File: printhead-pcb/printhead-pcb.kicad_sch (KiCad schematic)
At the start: 22 parts, among them Q1 2N3819, Q2 BSS138, Q3 2N3819, Q4 BSS138, U1 NE555D, U2 NE555D

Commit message: power fans, sensors
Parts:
- removed C1, C4, C6: 100n, Capacitor_SMD:C_0603_1608Metric, symbol Device:C
- removed C2, C5: 700p, Capacitor_SMD:C_0603_1608Metric, symbol Device:C
- removed C3: 2.2u, Capacitor_SMD:C_1210_3225Metric, symbol Device:C
- removed D1, D2, D3, D4: 1N4148W, Diode_SMD:D_SOD-123, symbol Diode:1N4148W
- removed Q1, Q3: 2N3819, Package_DIP:DIP-8_W7.62mm_SMDSocket_SmallPads, symbol Transistor_FET:2N3819
- removed Q2, Q4: BSS138, Package_TO_SOT_SMD:SOT-23, symbol Transistor_FET:BSS138
- removed R3, R5: 5k7, Resistor_SMD:R_0603_1608Metric, symbol Device:R
- removed R4, R6: 1k, Resistor_SMD:R_0603_1608Metric, symbol Device:R
- removed U1, U2: NE555D, Package_SO:SOIC-8_3.9x4.9mm_P1.27mm, symbol Timer:NE555D
- added U6: PCA9536D, Package_SO:SOIC-8_3.9x4.9mm_P1.27mm, symbol Interface_Expansion:PCA9536D
- R1, R2: value 1k -> 10k; footprint Resistor_SMD:R_0603_1608Metric -> (none)
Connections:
- net +5V is gone; now on net +3V3: R1.1
- net +3V3: now reaches R2.1
- net +3V3: no longer R1.2
- net SCL: now reaches R2.2
- new net SDA: R1.2
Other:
- added sheet fans (fans.kicad_sch)
- added sheet pwr (pwr.kicad_sch)
- added sheet sensors (sensors.kicad_sch)

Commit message: circuit finished?
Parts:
- removed U6: PCA9536D, Package_SO:SOIC-8_3.9x4.9mm_P1.27mm, symbol Interface_Expansion:PCA9536D
- added C10: 0.22µF, Capacitor_SMD:C_0402_1005Metric, symbol Device:C
- added C11: 0.1µF, Capacitor_SMD:C_0402_1005Metric, symbol Device:C
- added C9: 1µF, Capacitor_SMD:C_0402_1005Metric, symbol Device:C
- added D1: GREEN, LED_SMD:LED_0805_2012Metric, symbol Device:LED
- added L6: L, Inductor_SMD:L_0402_1005Metric, symbol Device:L
- added R17: 1k, Resistor_SMD:R_0402_1005Metric, symbol Device:R
- R1, R2: footprint (none) -> Resistor_SMD:R_0402_1005Metric
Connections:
- net +3V3: now also D1.2 (A), L6.1
- new net: D1.1 (K), R17.1
- new net: C10.1, C11.1, C9.1, L6.2
- new net GND: C10.2, C11.2, C9.2, R17.2
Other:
- removed sheet pwr
- added sheet io (io.kicad_sch)
- title: (none) -> Printhead PCB
- moved on the sheet: R1, R2

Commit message: layout
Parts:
- removed C9: 1µF, Capacitor_SMD:C_0402_1005Metric, symbol Device:C
- removed L6: L, Inductor_SMD:L_0402_1005Metric, symbol Device:L
- added C1, C2: 0.1µF, Capacitor_SMD:CP_Elec_5x3, symbol Device:C_Polarized
- added C3: 0.22µF, Capacitor_SMD:C_0402_1005Metric, symbol Device:C
- added C5: 0.1µF, Capacitor_SMD:C_0402_1005Metric, symbol Device:C
- added H1, H2, H3, H4: MountingHole_Pad, MountingHole:MountingHole_2.2mm_M2_Pad_TopBottom, symbol Mechanical:MountingHole_Pad
- added J1: PWR, Connector_JST:JST_EH_S5B-EH_1x05_P2.50mm_Horizontal, symbol Connector:Conn_01x05_Male
- renumbered C10 to C4, C11 to C6, R17 to R1, R1 to R2, R2 to R3
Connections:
- net +3V3: now also C4.1, C6.1, C2.1, J1.1 (Pin_1)
- net GND: now also C1.2, C2.2, C3.2, C5.2, H1.1, H2.1, H3.1, H4.1, J1.2 (Pin_2)
- net SCL: now also J1.5 (Pin_5)
- net SDA: now also J1.4 (Pin_4)
- new net +12V: C1.1, C3.1, C5.1, J1.3 (Pin_3)
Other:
- moved on the sheet: C4, C6, D1, R1, R2, R3

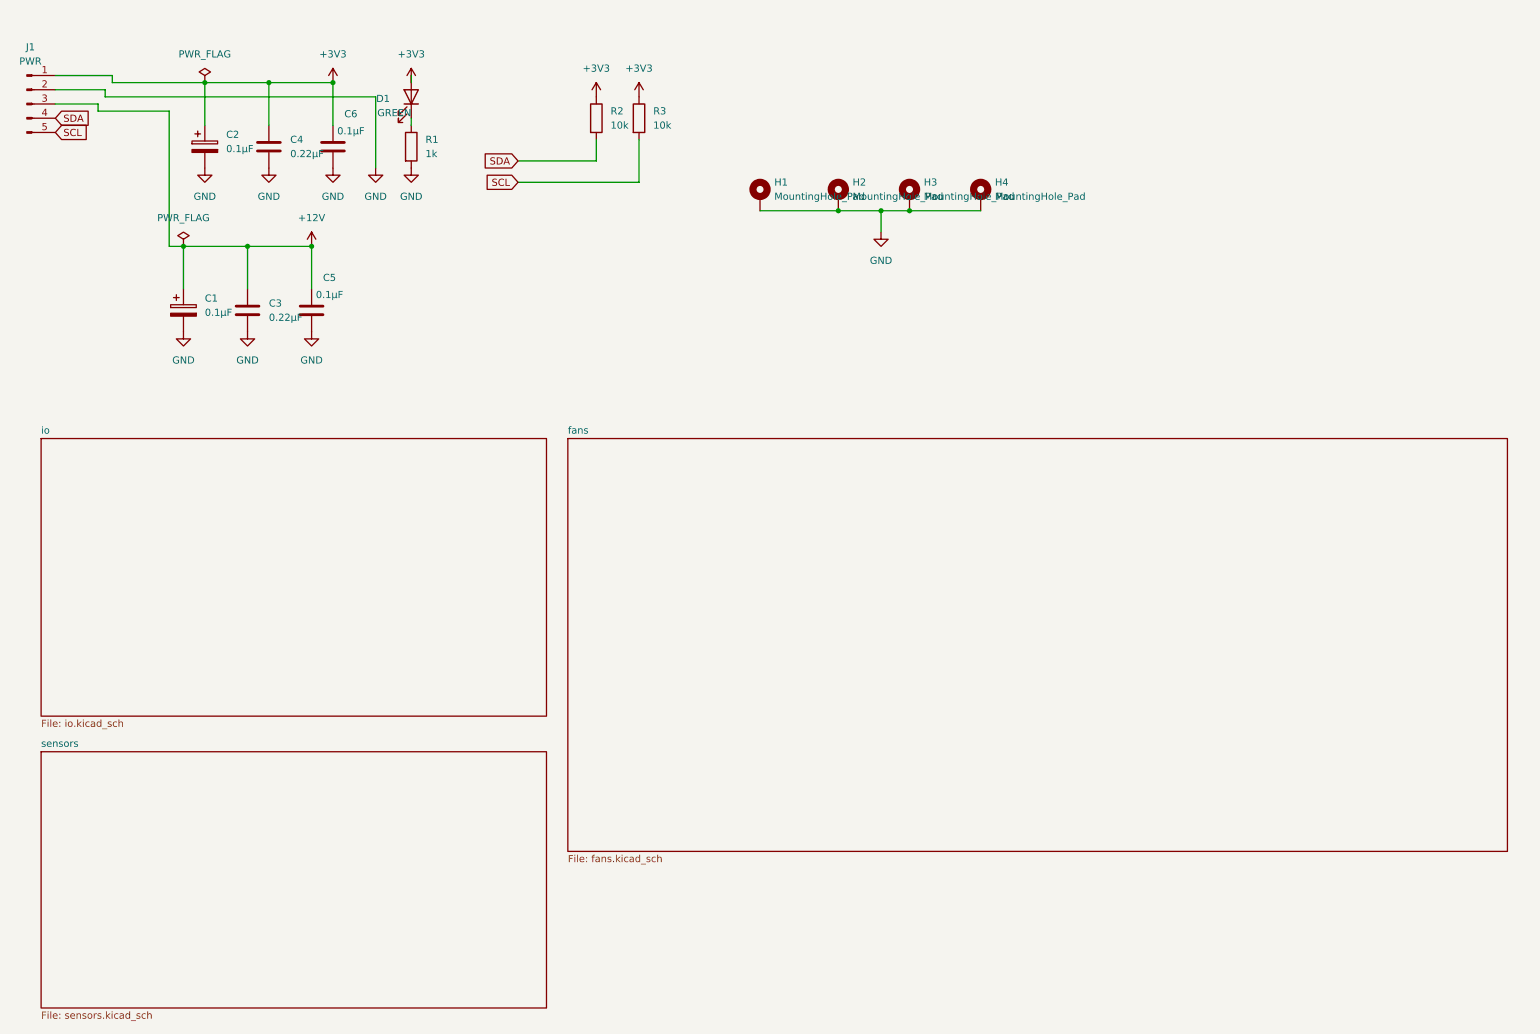
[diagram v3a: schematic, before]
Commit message: added PCA9615 chip for differiantial I2C Communication
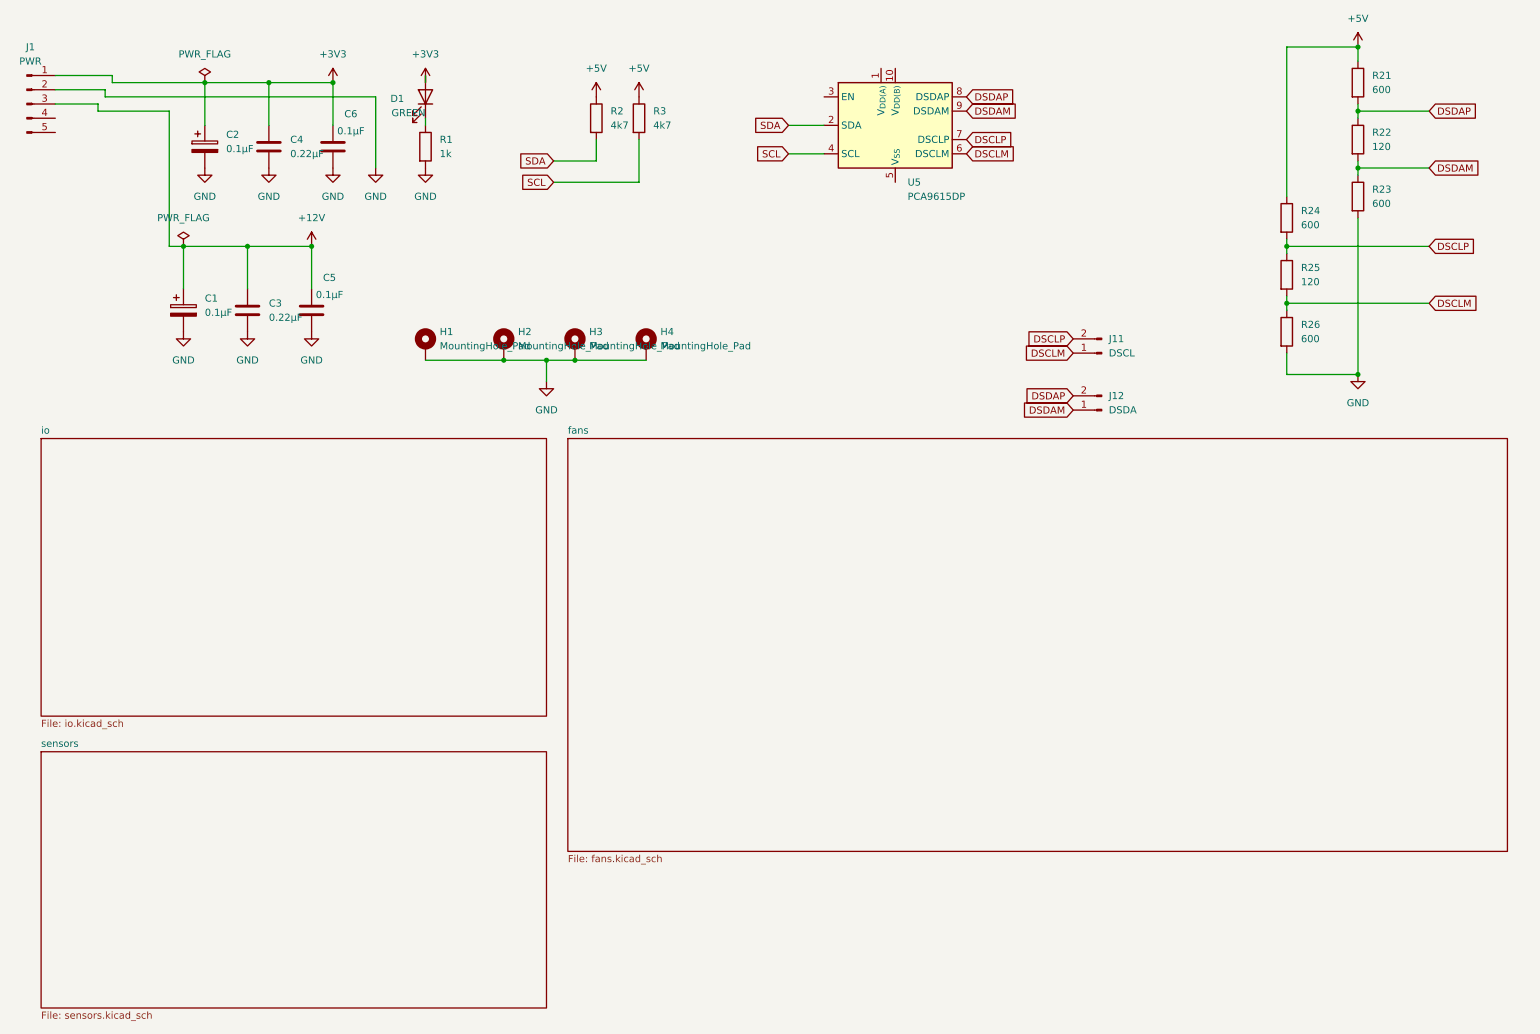
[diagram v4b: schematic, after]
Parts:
- added J11: DSCL, symbol Connector:Conn_01x02_Pin
- added J12: DSDA, symbol Connector:Conn_01x02_Pin
- added R21, R23, R24, R26: 600, Resistor_SMD:R_0402_1005Metric, symbol Device:R
- added R22, R25: 120, Resistor_SMD:R_0402_1005Metric, symbol Device:R
- added U5: PCA9615DP, Package_SO:TSSOP-10_3x3mm_P0.5mm, symbol Interface:PCA9615DP
- R2, R3: value 10k -> 4k7
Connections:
- net +3V3: no longer R2.1, R3.1
- net GND: now also R23.2, R26.2
- net SCL: now also U5.4 (SCL); no longer J1.5 (Pin_5)
- net SDA: now also U5.2 (SDA); no longer J1.4 (Pin_4)
- new net +5V: R2.1, R21.1, R24.1, R3.1
- new net DSCLM: J11.1 (Pin_1), R25.2, R26.1, U5.6 (DSCLM)
- new net DSCLP: J11.2 (Pin_2), R24.2, R25.1, U5.7 (DSCLP)
- new net DSDAM: J12.1 (Pin_1), R22.2, R23.1, U5.9 (DSDAM)
- new net DSDAP: J12.2 (Pin_2), R21.2, R22.1, U5.8 (DSDAP)
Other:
- moved on the sheet: D1, H1, H2, H3, H4, R1

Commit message: add pwr, gnd 5V for di2c chip
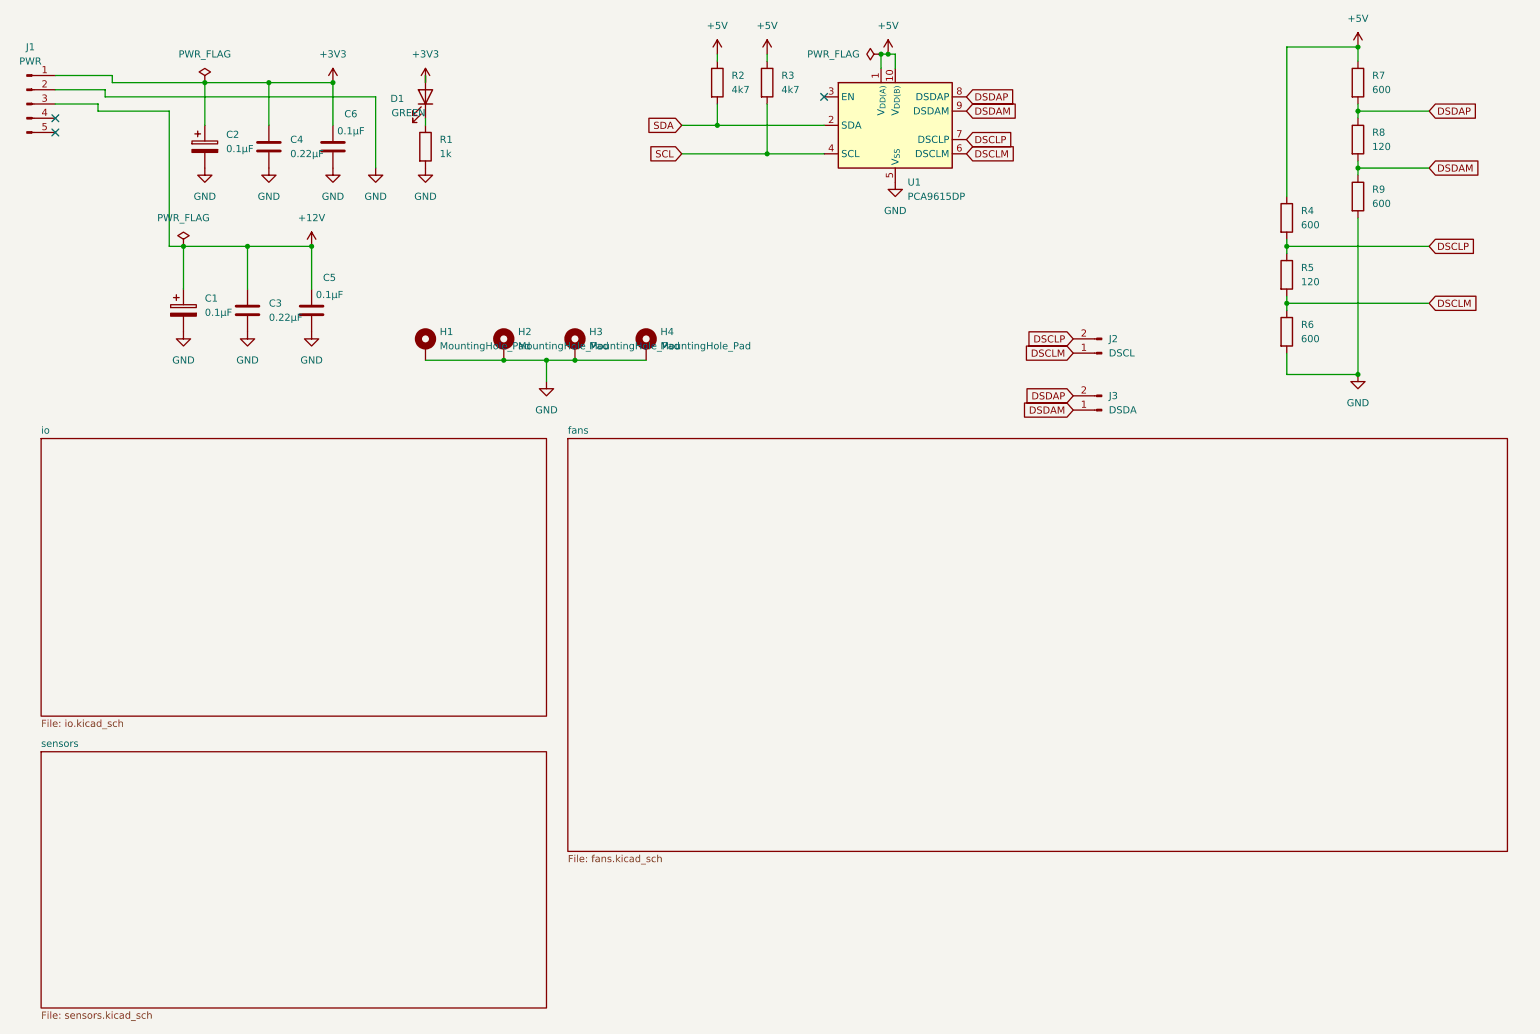
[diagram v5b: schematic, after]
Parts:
- renumbered J11 to J2, J12 to J3, R24 to R4, R25 to R5, R26 to R6, R21 to R7, R22 to R8, R23 to R9, U5 to U1
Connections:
- net +5V: now also U1.1 (V_{DD(A)}), U1.10 (V_{DD(B)})
- net GND: now also U1.5 (V_{SS})
- no-connect marks 0 -> 3
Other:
- moved on the sheet: R2, R3

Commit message: added voltage converter
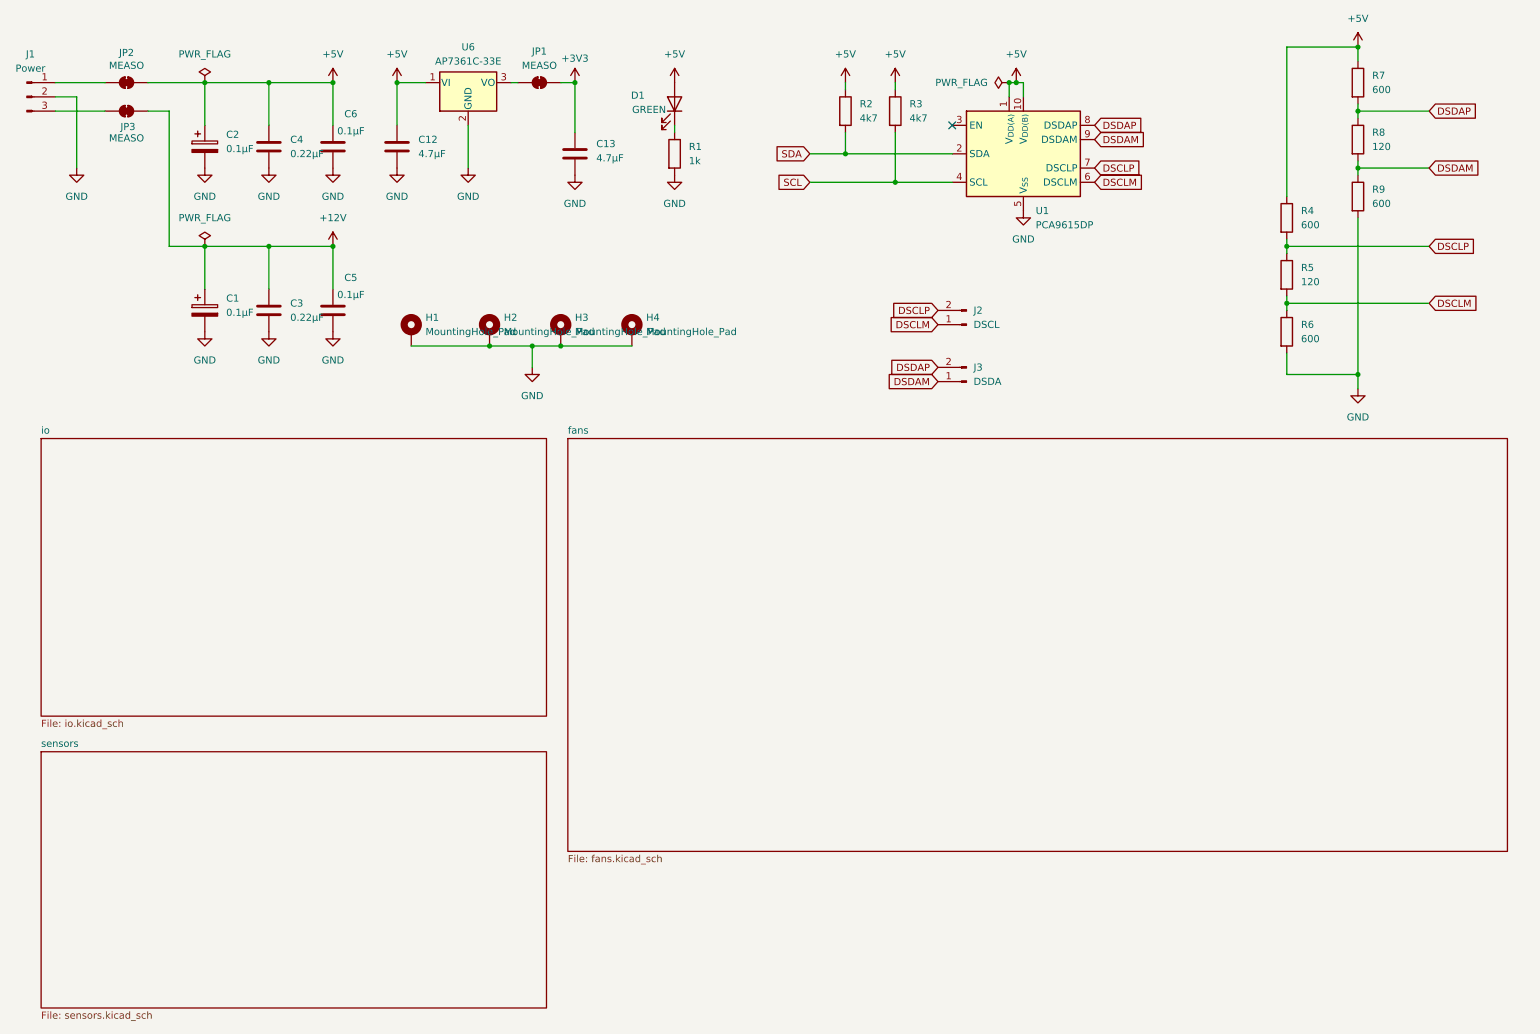
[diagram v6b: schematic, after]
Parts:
- removed J1: PWR, Connector_JST:JST_EH_S5B-EH_1x05_P2.50mm_Horizontal, symbol Connector:Conn_01x05_Male
- added C12, C13: 4.7µF, Capacitor_SMD:C_0402_1005Metric, symbol Device:C
- added J1: Power, symbol Connector:Conn_01x03_Pin
- added JP1, JP2, JP3: MEASO, symbol Jumper:SolderJumper_2_Bridged
- added U6: AP7361C-33E, Package_TO_SOT_SMD:SOT-223-3_TabPin2, symbol Regulator_Linear:AP7361C-33E
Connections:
- net +12V: now also JP3.2 (B)
- net +3V3: now also C13.1, JP1.2 (B); no longer C2.1, C4.1, C6.1, D1.2 (A)
- net +5V: now also C2.1, C4.1, C6.1, D1.2 (A), C12.1, JP2.2 (B), U6.1 (VI)
- net GND: now also C12.2, C13.2, J1.2 (Pin_2), U6.2 (GND)
- new net: J1.1 (Pin_1), JP2.1 (A)
- new net: JP1.1 (A), U6.3 (VO)
- new net: J1.3 (Pin_3), JP3.1 (A)
- no-connect marks 3 -> 1
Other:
- moved on the sheet: C1, C3, C5, D1, H1, H2, H3, H4, J2, J3, R1, R2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

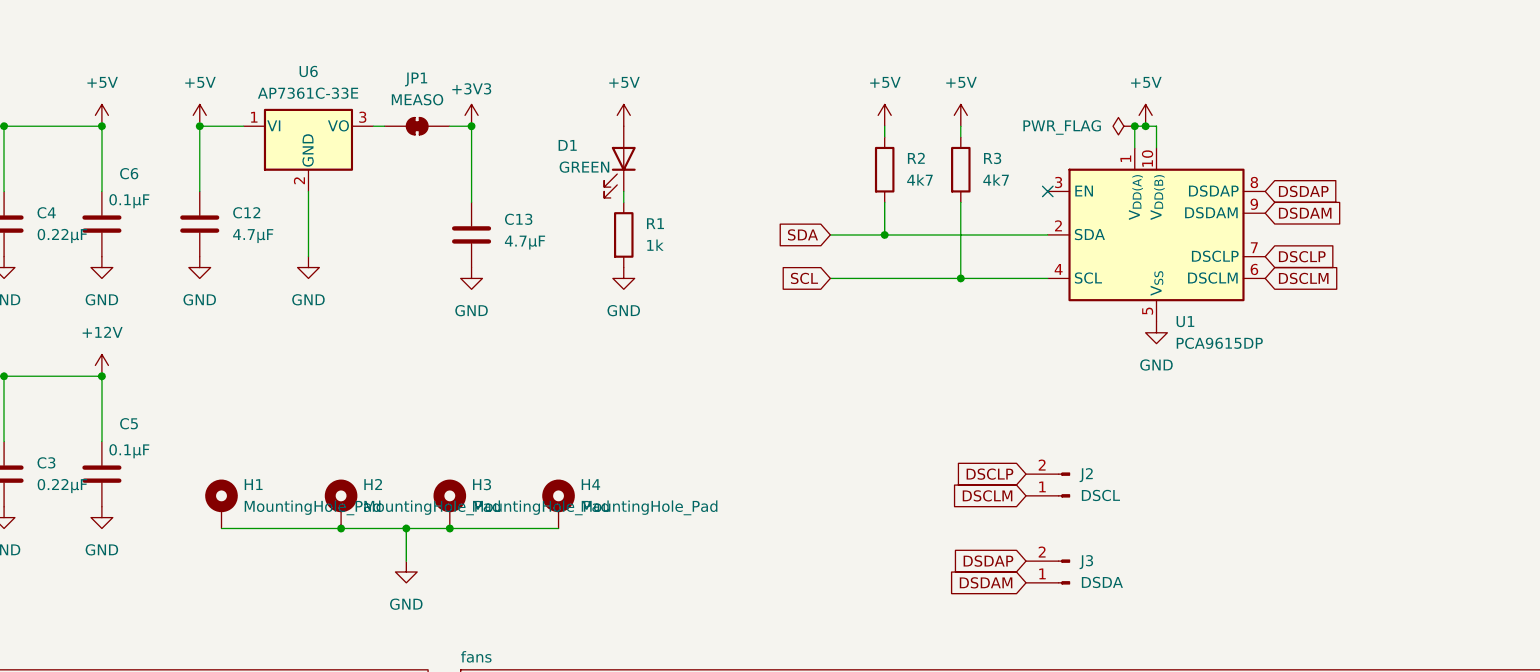
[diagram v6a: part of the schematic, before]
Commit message: worked through errors and added data sheets
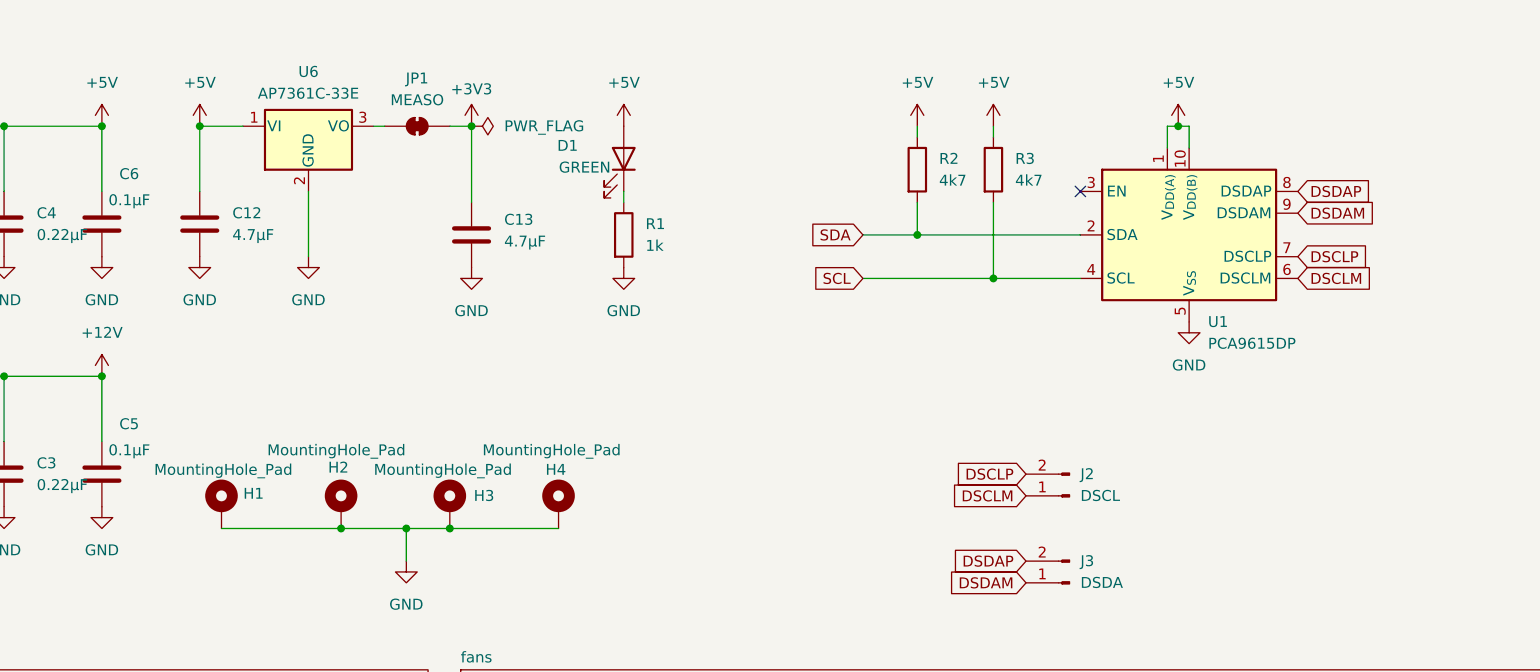
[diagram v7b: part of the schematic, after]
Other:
- moved on the sheet: R2, R3, U1
